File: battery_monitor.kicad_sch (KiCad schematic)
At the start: 0 parts

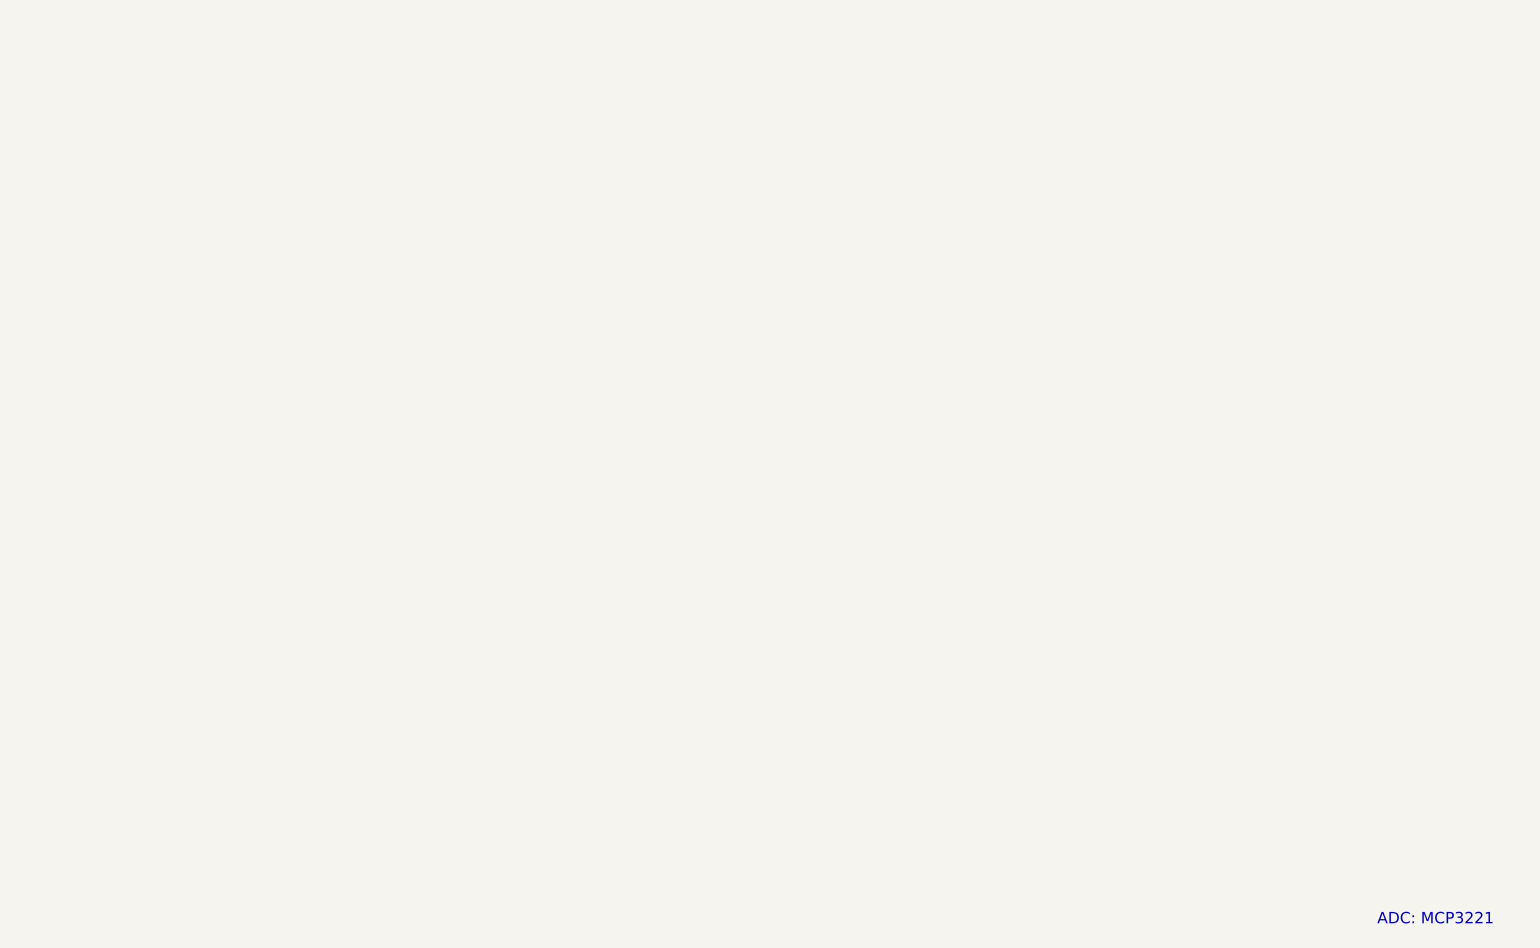
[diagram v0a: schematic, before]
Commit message: Added thruster battery monitoring circuit
There is no footprint assigned for an I2C isolator and resistors yet
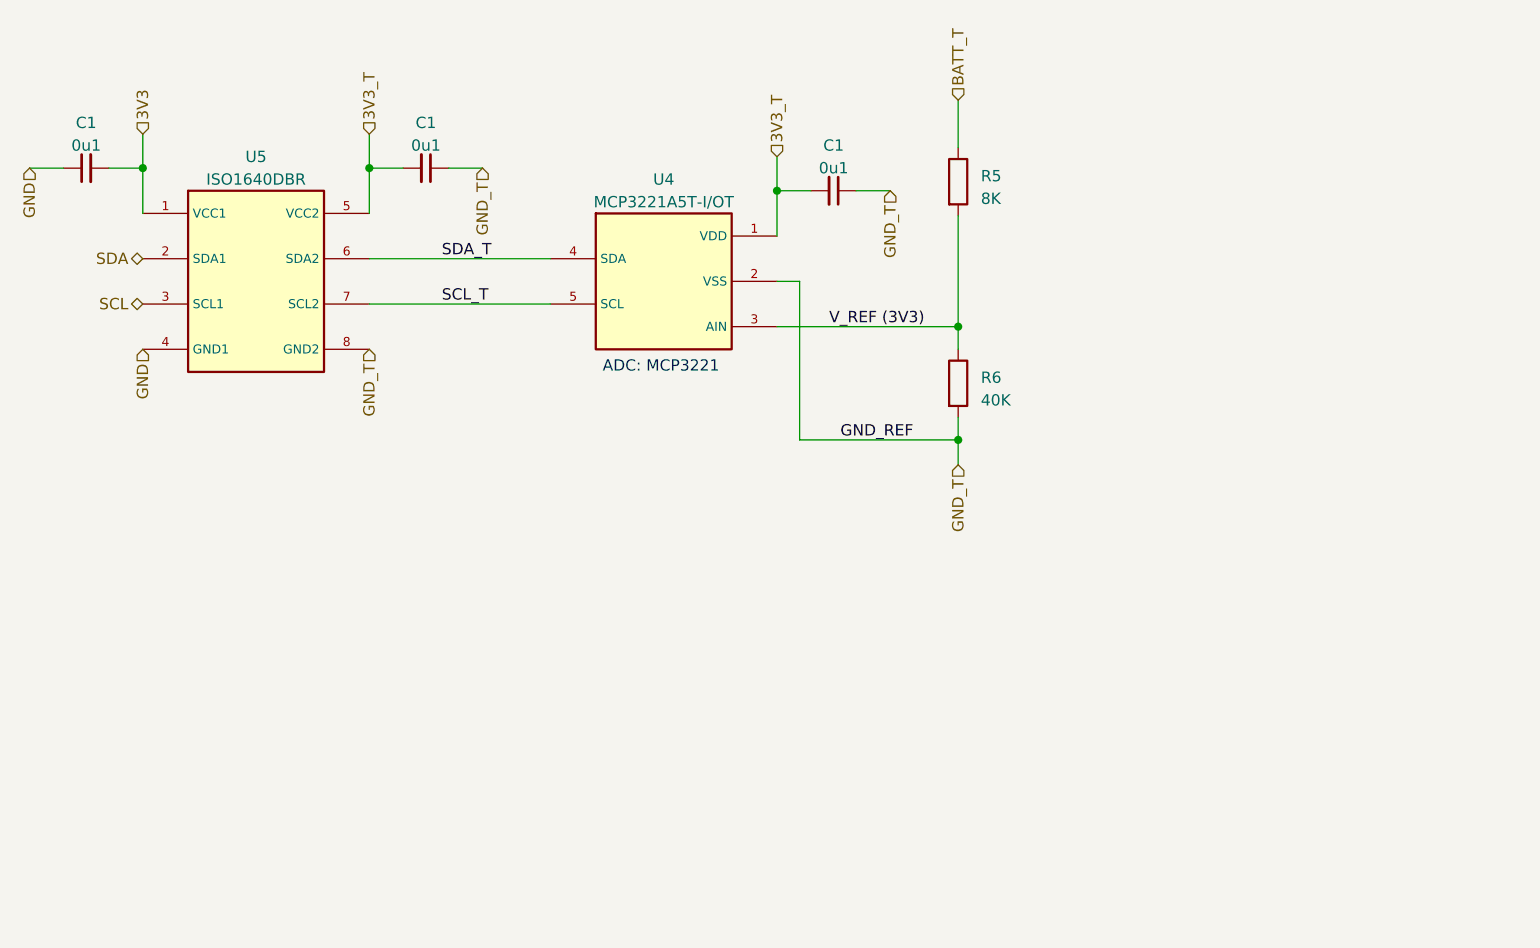
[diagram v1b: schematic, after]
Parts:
- added C1 (x3): 0u1, Capacitor_SMD:C_0402_1005Metric, symbol Device:C_Small
- added R5: 8K, symbol Device:R
- added R6: 40K, symbol Device:R
- added U4: MCP3221A5T-I/OT, Crush_Mainboard_Footprints:SOT95P280X145-5N, symbol Crush_MainBoard_Symbols:MCP3221A5T-I/OT
- added U5: ISO1640DBR, symbol Crush_MainBoard_Symbols:ISO1640DBR
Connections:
- new net 3V3: C1.2, U5.1 (VCC1)
- new net 3V3_T: C1.2, C1.2, U4.1 (VDD), U5.5 (VCC2)
- new net BATT_T: R5.1
- new net GND: C1.1, U5.4 (GND1)
- new net GND_T: C1.1, C1.1, R6.2, U4.2 (VSS), U5.8 (GND2)
- new net SCL: U5.3 (SCL1)
- new net SCL_T: U4.5 (SCL), U5.7 (SCL2)
- new net SDA: U5.2 (SDA1)
- new net SDA_T: U4.4 (SDA), U5.6 (SDA2)
- new net V_REF (3V3): R5.2, R6.1, U4.3 (AIN)

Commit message: fixed some minor error
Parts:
- R5: value 8K -> 40K
- R6: value 40K -> 10K
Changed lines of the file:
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@@
       (effects (font (size 1.27 1.27)) (justify left))
     )
-    (property "Value" "8K" (at 127 26.289 0)
+    (property "Value" "40K" (at 127 26.289 0)
       (effects (font (size 1.27 1.27)) (justify left))
     )
@@
       (effects (font (size 1.27 1.27)) (justify left))
     )
-    (property "Value" "40K" (at 127 48.895 0)
+    (property "Value" "10K" (at 127 48.895 0)
       (effects (font (size 1.27 1.27)) (justify left))
     )

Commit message: added electrical side battery monitor in case we don't use Teensy's ADC
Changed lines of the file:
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@@
+    (effects (font (size 1.27 1.27)) (justify left bottom))
+  )
+  (label "16V8 (MAX)" (at 124.46 19.05 0) (fields_autoplaced)
     (effects (font (size 1.27 1.27)) (justify left bottom))
   )

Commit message: Added diode and header for remaining pins, fixed signal battery monitor
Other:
- moved on the sheet: R5
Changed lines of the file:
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@@
     (stroke (width 0) (type default))
   )
-  (wire (pts (xy 124.46 28.194) (xy 124.46 40.64))
+  (wire (pts (xy 124.46 34.29) (xy 124.46 40.64))
     (stroke (width 0) (type default))
   )
@@
     (stroke (width 0) (type default))
   )
-  (wire (pts (xy 124.46 15.24) (xy 124.46 20.574))
+  (wire (pts (xy 124.46 15.24) (xy 124.46 26.67))
     (stroke (width 0) (type default))
   )
@@
     (effects (font (size 1.27 1.27)) (justify left bottom))
   )
-  (label "16V8 (MAX)" (at 124.46 19.05 0) (fields_autoplaced)
+  (label "16V8 (MAX)" (at 124.46 21.844 0) (fields_autoplaced)
     (effects (font (size 1.27 1.27)) (justify left bottom))
   )
@@
     (effects (font (size 1.27 1.27)) (justify left))
   )
-  (symbol (lib_id "Device:R") (at 124.46 24.384 0) (unit 1)
+  (symbol (lib_id "Device:R") (at 124.46 30.48 0) (unit 1)
     (in_bom yes) (on_board yes) (dnp no) (fields_autoplaced)
-    (property "Reference" "R5" (at 127 23.749 0)
+    (property "Reference" "R5" (at 127 29.845 0)
       (effects (font (size 1.27 1.27)) (justify left))
     )
-    (property "Value" "40K" (at 127 26.289 0)
+    (property "Value" "40K" (at 127 32.385 0)
       (effects (font (size 1.27 1.27)) (justify left))
     )
-    (property "Footprint" "" (at 122.682 24.384 90)
+    (property "Footprint" "" (at 122.682 30.48 90)
       (effects (font (size 1.27 1.27)) hide)
     )
-    (property "Datasheet" "~" (at 124.46 24.384 0)
+    (property "Datasheet" "~" (at 124.46 30.48 0)
       (effects (font (size 1.27 1.27)) hide)
     )

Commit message: Changed resistor and capacitor footprints to 0603
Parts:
- C1: footprint Capacitor_SMD:C_0402_1005Metric -> Capacitor_SMD:C_0603_1608Metric_Pad1.08x0.95mm_HandSolder
- R5, R6: footprint (none) -> Resistor_SMD:R_0603_1608Metric_Pad0.98x0.95mm_HandSolder
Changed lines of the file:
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@@
       (effects (font (size 1.27 1.27)) (justify left))
     )
-    (property "Footprint" "" (at 122.682 30.48 90)
+    (property "Footprint" "Resistor_SMD:R_0603_1608Metric_Pad0.98x0.95mm_HandSolder" (at 122.682 30.48 90)
       (effects (font (size 1.27 1.27)) hide)
     )
@@
       (effects (font (size 1.27 1.27)))
     )
-    (property "Footprint" "Capacitor_SMD:C_0402_1005Metric" (at 64.77 22.86 0)
+    (property "Footprint" "Capacitor_SMD:C_0603_1608Metric_Pad1.08x0.95mm_HandSolder" (at 64.77 22.86 0)
       (effects (font (size 1.27 1.27)) hide)
     )
@@
       (effects (font (size 1.27 1.27)))
     )
-    (property "Footprint" "Capacitor_SMD:C_0402_1005Metric" (at 26.67 22.86 0)
+    (property "Footprint" "Capacitor_SMD:C_0603_1608Metric_Pad1.08x0.95mm_HandSolder" (at 26.67 22.86 0)
       (effects (font (size 1.27 1.27)) hide)
     )
@@
       (effects (font (size 1.27 1.27)) (justify left))
     )
-    (property "Footprint" "" (at 122.682 46.99 90)
+    (property "Footprint" "Resistor_SMD:R_0603_1608Metric_Pad0.98x0.95mm_HandSolder" (at 122.682 46.99 90)
       (effects (font (size 1.27 1.27)) hide)
     )
@@
       (effects (font (size 1.27 1.27)))
     )
-    (property "Footprint" "Capacitor_SMD:C_0402_1005Metric" (at 110.49 25.4 0)
+    (property "Footprint" "Capacitor_SMD:C_0603_1608Metric_Pad1.08x0.95mm_HandSolder" (at 110.49 25.4 0)
       (effects (font (size 1.27 1.27)) hide)
     )

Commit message: Added connection to the power board; and the remaining footprints
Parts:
- U5: footprint (none) -> Crush_Mainboard_Footprints:SOIC127P1030X265-16N
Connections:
- net 3V3: now also U5.3 (VCC1); no longer U5.1 (VCC1)
- net 3V3_T: now also U5.14 (VCC2); no longer U5.5 (VCC2)
- net GND: now also U5.7 (GND1); no longer U5.4 (GND1)
- net GND_T: now also U5.9 (GND2); no longer U5.8 (GND2)
- net SCL: now also U5.6 (SCL1); no longer U5.3 (SCL1)
- net SCL_T: now also U5.11 (SCL2); no longer U5.7 (SCL2)
- net SDA: now also U5.5 (SDA1); no longer U5.2 (SDA1)
- net SDA_T: now also U5.12 (SDA2); no longer U5.6 (SDA2)
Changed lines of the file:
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@@
       (effects (font (size 1.27 1.27)))
     )
-    (property "Footprint" "" (at 45.72 44.45 0)
+    (property "Footprint" "Crush_Mainboard_Footprints:SOIC127P1030X265-16N" (at 45.72 44.45 0)
       (effects (font (size 1.27 1.27)) hide)
     )
@@
       (effects (font (size 1.27 1.27)) hide)
     )
-    (pin "1")
-    (pin "2")
+    (pin "11")
+    (pin "12")
+    (pin "14")
     (pin "3")
-    (pin "4")
     (pin "5")
     (pin "6")
     (pin "7")
-    (pin "8")
+    (pin "9")
     (instances
       (project "crush-main-board"

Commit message: Add battery monitoring circuit using INA233
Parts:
- removed C1: 0u1, Capacitor_SMD:C_0603_1608Metric_Pad1.08x0.95mm_HandSolder, symbol Device:C_Small
- removed R5: 40K, Resistor_SMD:R_0603_1608Metric_Pad0.98x0.95mm_HandSolder, symbol Device:R
- removed R6: 10K, Resistor_SMD:R_0603_1608Metric_Pad0.98x0.95mm_HandSolder, symbol Device:R
- removed U4: MCP3221A5T-I/OT, Crush_Mainboard_Footprints:SOT95P280X145-5N, symbol Crush_MainBoard_Symbols:MCP3221A5T-I/OT
- added U1: INA233, Package_SO:VSSOP-10_3x3mm_P0.5mm, symbol Sensor_Energy:INA233
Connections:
- net 3V3_T: now also U1.6 (VS)
- net BATT_T: now also U1.10 (Vin+), U1.8 (Vbus), U1.9 (Vin-)
- net GND_T: now also U1.1 (A1), U1.2 (A0), U1.7 (GND)
- net SCL_T: now also U1.5 (SCL)
- net SDA_T: now also U1.4 (SDA)
- no-connect marks 0 -> 1
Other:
- note added: "I2C Addr: 0x40"
- note removed: "ADC: MCP3221"
